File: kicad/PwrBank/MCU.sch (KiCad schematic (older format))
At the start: 2 parts

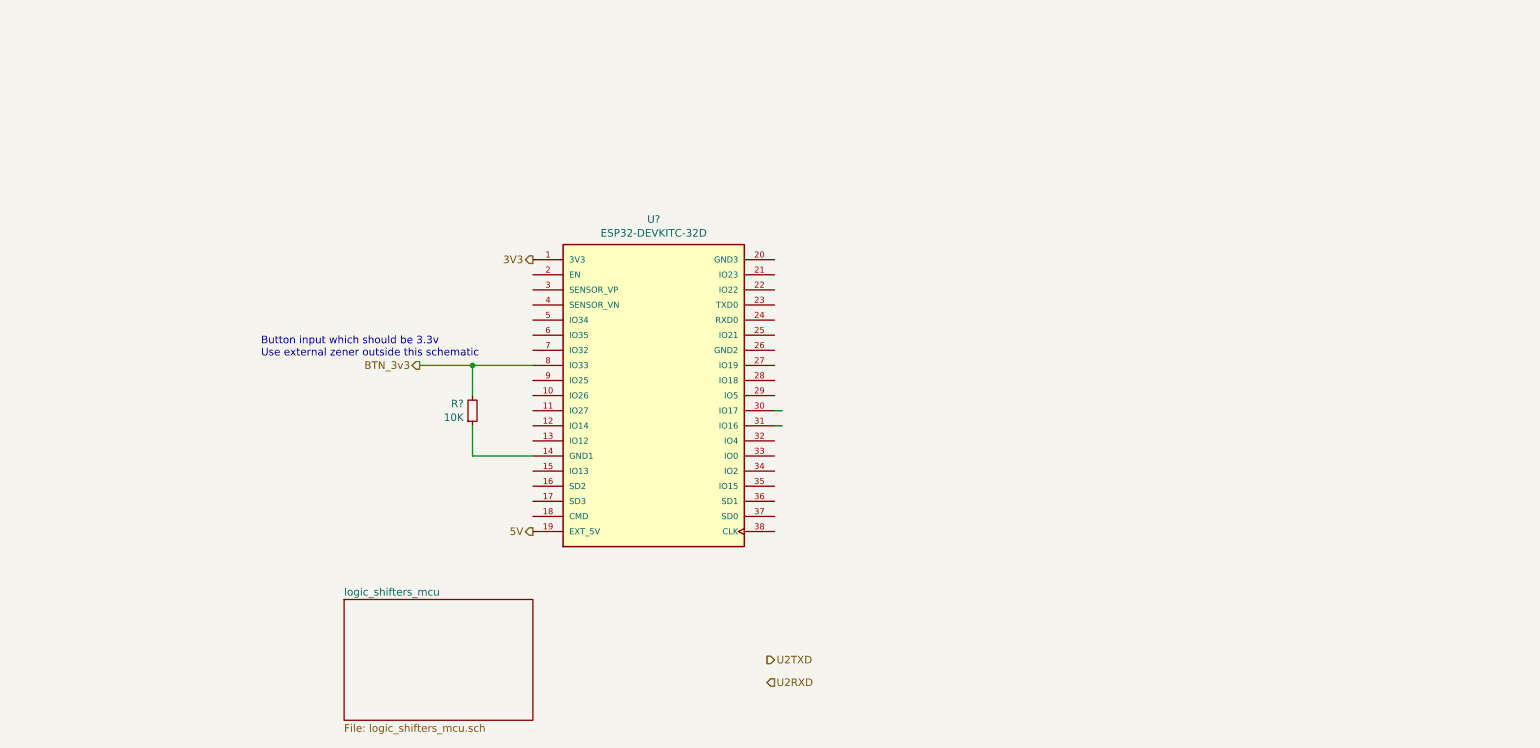
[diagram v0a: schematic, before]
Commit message: Working on/off system with safe shutdown and deepsleep inbetween
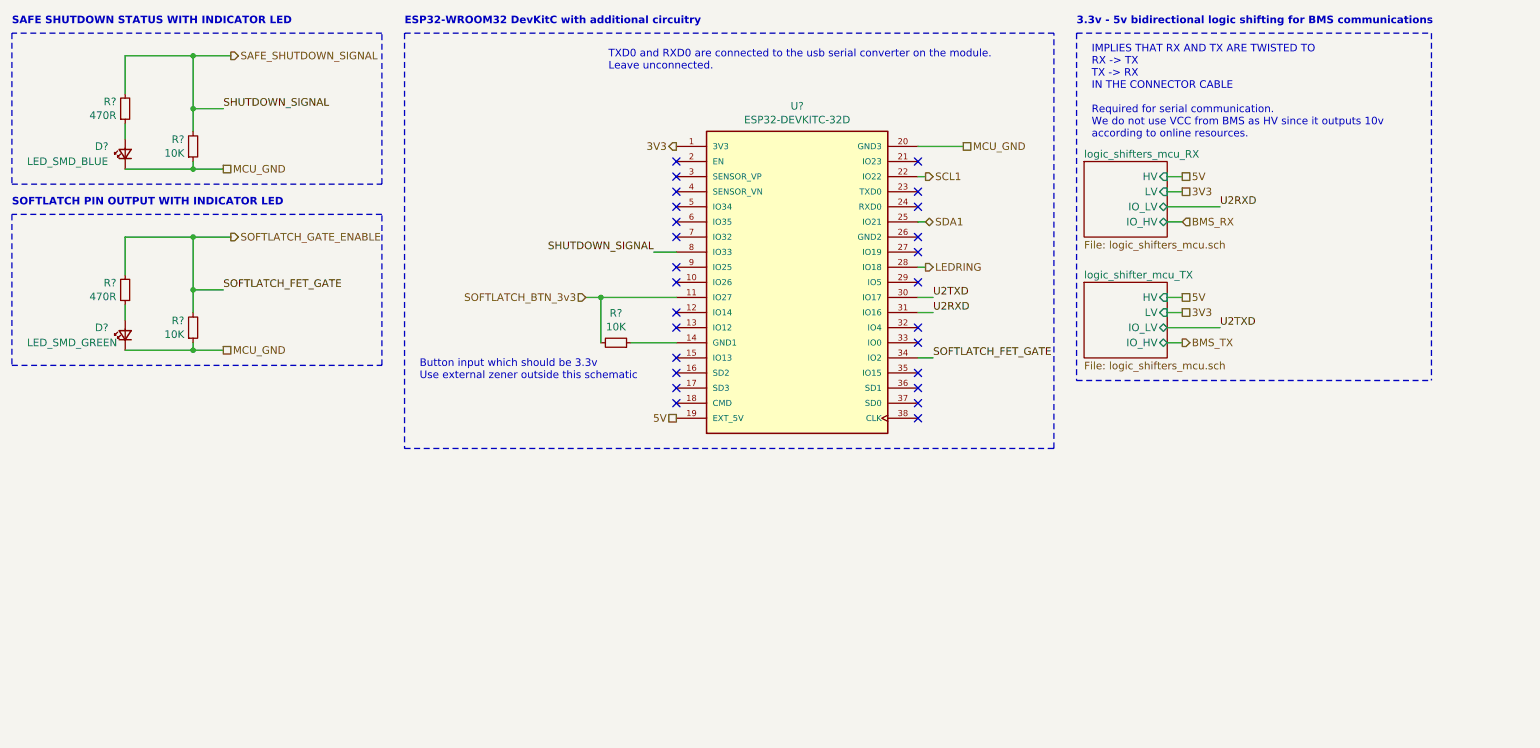
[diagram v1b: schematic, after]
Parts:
- added D?: LED_SMD_GREEN, symbol Device:LED_Small
- added D?: LED_SMD_BLUE, symbol Device:LED_Small
- added R? (x2): 10K, symbol Device:R_Small
- added R? (x2): 470R, symbol Device:R_Small
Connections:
- net labels added: BMS_RX, BMS_TX, LEDRING, MCU_GND, SAFE_SHUTDOWN_SIGNAL, SCL1, SDA1, SHUTDOWN_SIGNAL, SOFTLATCH_BTN_3v3, SOFTLATCH_FET_GATE, SOFTLATCH_GATE_ENABLE
- net labels removed: BTN_3v3
- wire segments 7 -> 40
- no-connect marks 0 -> 26
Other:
- note added: "3.3v - 5v bidirectional logic shifting for BMS communications"
- note added: "ESP32-WROOM32 DevKitC with additional circuitry\n"
- note added: "IMPLIES THAT RX AND TX ARE TWISTED TO\nRX -> TX\nTX -> RX\nIN THE CONNECTOR CABLE\n\nRequired for serial communication.\nWe do not use VCC from BMS as HV since it outputs 10v\naccording to online resources."
- note added: "SAFE SHUTDOWN STATUS WITH INDICATOR LED"
- note added: "SOFTLATCH PIN OUTPUT WITH INDICATOR LED"
- note added: "TXD0 and RXD0 are connected to the usb serial converter on the module.\nLeave unconnected."
- moved on the sheet: R?, U?

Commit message: UPDATE KICAD SOURCEFILES
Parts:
- R11, R12, R13, R14, R15: renamed from R?; footprint (none) -> Resistor_SMD:R_0805_2012Metric_Pad1.20x1.40mm_HandSolder
- U2: renamed from U?; footprint MODULE_ESP32-DEVKITC-32D -> ESP32-DEVKITC-32D:MODULE_ESP32-DEVKITC-32D
- gave numbers to parts that had none: 2
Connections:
- net 3V3 renamed +3V3
- net 5V renamed +5V
- net MCU_GND renamed GND
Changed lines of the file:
@@
 $Descr A4 11693 8268
 encoding utf-8
-Sheet 7 9
+Sheet 6 8
 Title "ESP32_Devkit_Addons"
 Date "2021-07-17"
@@
 $EndDescr
 $Comp
-L ESP32-DEVKITC-32D:ESP32-DEVKITC-32D U?
+L ESP32-DEVKITC-32D:ESP32-DEVKITC-32D U2
 U 1 1 60F2EDCB
 P 6050 2900
-F 0 "U?" H 6050 4067 50  0000 C CNN
+F 0 "U2" H 6050 4067 50  0000 C CNN
 F 1 "ESP32-DEVKITC-32D" H 6050 3976 50  0000 C CNN
-F 2 "MODULE_ESP32-DEVKITC-32D" H 6050 2900 50  0001 L BNN
+F 2 "ESP32-DEVKITC-32D:MODULE_ESP32-DEVKITC-32D" H 6050 2900 50  0001 L BNN
 F 3 "" H 6050 2900 50  0001 L BNN
 F 4 "4" H 6050 2900 50  0001 L BNN "PARTREV"
@@
 BMS_TX
 $Comp
-L Device:R_Small R?
+L Device:R_Small R15
 U 1 1 60F3049F
 P 4850 3300
-F 0 "R?" V 5046 3300 50  0000 C CNN
+F 0 "R15" V 5046 3300 50  0000 C CNN
 F 1 "10K" V 4955 3300 50  0000 C CNN
-F 2 "" H 4850 3300 50  0001 C CNN
+F 2 "Resistor_SMD:R_0805_2012Metric_Pad1.20x1.40mm_HandSolder" H 4850 3300 50  0001 C CNN
 F 3 "~" H 4850 3300 50  0001 C CNN
 	1    4850 3300
@@
 Text Notes 3550 3550 0    50   ~ 0
 Button input which should be 3.3v\nUse external zener outside this schematic
-Text HLabel 5250 3800 0    50   UnSpc ~ 0
-5V
-Text HLabel 5250 2000 0    50   Output ~ 0
-3V3
-$Sheet
-S 7950 2100 550  500
-U 60F3980E
-F0 "logic_shifters_mcu_RX" 50
-F1 "logic_shifters_mcu.sch" 50
-F2 "IO_LV" B R 8500 2400 50
-F3 "IO_HV" B R 8500 2500 50
-F4 "HV" I R 8500 2200 50
-F5 "LV" I R 8500 2300 50
-$EndSheet
-Text HLabel 8600 2200 2    50   UnSpc ~ 0
-5V
 Wire Wire Line
 	8600 2200 8500 2200
-Text HLabel 8600 3000 2    50   UnSpc ~ 0
-5V
 Wire Wire Line
 	8600 3000 8500 3000
-Text HLabel 8600 3100 2    50   UnSpc ~ 0
-3V3
 Wire Wire Line
 	8600 3100 8500 3100
-Text HLabel 8600 2300 2    50   UnSpc ~ 0
-3V3
 Wire Wire Line
 	8600 2300 8500 2300
@@
 Text Notes 7900 1200 0    50   ~ 10
 3.3v - 5v bidirectional logic shifting for BMS communications
-Text HLabel 7150 2000 2    50   UnSpc ~ 0
-MCU_GND
 Wire Wire Line
 	7150 2000 6850 2000
@@
 	4650 3000 4750 3000
 Wire Wire Line
-	5250 3300 4950 3300
+	5250 3300 5050 3300
 Wire Wire Line
 	4750 3300 4750 3000
@@
 	4750 3000 5250 3000
 $Comp
-L Device:LED_Small D?
+L Device:LED_Small D3
 U 1 1 60F6DAA2
 P 1600 2050
-F 0 "D?" V 1650 2250 50  0000 R CNN
+F 0 "D3" V 1650 2250 50  0000 R CNN
 F 1 "LED_SMD_BLUE" V 1550 2700 50  0000 R CNN
 F 2 "" V 1600 2050 50  0001 C CNN
@@
 Wire Wire Line
 	5100 2700 5250 2700
-Text HLabel 2250 2150 2    50   UnSpc ~ 0
-MCU_GND
 Text Label 2250 1750 0    50   ~ 0
 SHUTDOWN_SIGNAL
@@
 	2300 1400 2050 1400
 $Comp
-L Device:R_Small R?
+L Device:R_Small R13
 U 1 1 60F71BF4
 P 2050 2000
-F 0 "R?" H 1992 1954 50  0000 R CNN
+F 0 "R13" H 1992 1954 50  0000 R CNN
 F 1 "10K" H 1992 2045 50  0000 R CNN
-F 2 "" H 2050 2000 50  0001 C CNN
+F 2 "Resistor_SMD:R_0805_2012Metric_Pad1.20x1.40mm_HandSolder" H 2050 2000 50  0001 C CNN
 F 3 "~" H 2050 2000 50  0001 C CNN
 	1    2050 2000
@@
 	1600 2150 2050 2150
 $Comp
-L Device:R_Small R?
+L Device:R_Small R11
 U 1 1 60F80C8C
 P 1600 1750
-F 0 "R?" H 1542 1704 50  0000 R CNN
+F 0 "R11" H 1542 1704 50  0000 R CNN
 F 1 "470R" H 1542 1795 50  0000 R CNN
-F 2 "" H 1600 1750 50  0001 C CNN
+F 2 "Resistor_SMD:R_0805_2012Metric_Pad1.20x1.40mm_HandSolder" H 1600 1750 50  0001 C CNN
 F 3 "~" H 1600 1750 50  0001 C CNN
 	1    1600 1750
@@
 	6950 3400 6850 3400
 $Comp
-L Device:LED_Small D?
+L Device:LED_Small D4
 U 1 1 60F351C2
 P 1600 3250
-F 0 "D?" V 1650 3450 50  0000 R CNN
+F 0 "D4" V 1650 3450 50  0000 R CNN
 F 1 "LED_SMD_GREEN" V 1550 3900 50  0000 R CNN
 F 2 "" V 1600 3250 50  0001 C CNN
@@
 	0    -1   -1   0
 $EndComp
-Text HLabel 2250 3350 2    50   UnSpc ~ 0
-MCU_GND
 Text Label 2250 2950 0    50   ~ 0
 SOFTLATCH_FET_GATE
@@
 	2300 2600 2050 2600
 $Comp
-L Device:R_Small R?
+L Device:R_Small R14
 U 1 1 60F351CF
 P 2050 3200
-F 0 "R?" H 1992 3154 50  0000 R CNN
+F 0 "R14" H 1992 3154 50  0000 R CNN
 F 1 "10K" H 1992 3245 50  0000 R CNN
-F 2 "" H 2050 3200 50  0001 C CNN
+F 2 "Resistor_SMD:R_0805_2012Metric_Pad1.20x1.40mm_HandSolder" H 2050 3200 50  0001 C CNN
 F 3 "~" H 2050 3200 50  0001 C CNN
 	1    2050 3200
@@
 	1600 3350 2050 3350
 $Comp
-L Device:R_Small R?
+L Device:R_Small R12
 U 1 1 60F351DA
 P 1600 2950
-F 0 "R?" H 1542 2904 50  0000 R CNN
+F 0 "R12" H 1542 2904 50  0000 R CNN
 F 1 "470R" H 1542 2995 50  0000 R CNN
-F 2 "" H 1600 2950 50  0001 C CNN
+F 2 "Resistor_SMD:R_0805_2012Metric_Pad1.20x1.40mm_HandSolder" H 1600 2950 50  0001 C CNN
 F 3 "~" H 1600 2950 50  0001 C CNN
 	1    1600 2950
@@
 Text Notes 3450 1200 0    50   ~ 10
 ESP32-WROOM32 DevKitC with additional circuitry\n
+Wire Wire Line
+	5250 2000 5150 2000
+Wire Wire Line
+	5150 3800 5250 3800
+$Comp
+L power:GND #PWR027
+U 1 1 61034275
+P 7150 2000
+F 0 "#PWR027" H 7150 1750 50  0001 C CNN
+F 1 "GND" V 7155 1872 50  0000 R CNN
+F 2 "" H 7150 2000 50  0001 C CNN
+F 3 "" H 7150 2000 50  0001 C CNN
+	1    7150 2000
+	0    -1   -1   0
+$EndComp
+$Comp
+L power:GND #PWR023
+U 1 1 61035069
+P 2250 2150
+F 0 "#PWR023" H 2250 1900 50  0001 C CNN
+F 1 "GND" V 2255 2022 50  0000 R CNN
+F 2 "" H 2250 2150 50  0001 C CNN
+F 3 "" H 2250 2150 50  0001 C CNN
+	1    2250 2150
+	0    -1   -1   0
+$EndComp
+$Comp
+L power:GND #PWR024
+U 1 1 61035606
+P 2250 3350
+F 0 "#PWR024" H 2250 3100 50  0001 C CNN
+F 1 "GND" V 2255 3222 50  0000 R CNN
+F 2 "" H 2250 3350 50  0001 C CNN
+F 3 "" H 2250 3350 50  0001 C CNN
+	1    2250 3350
+	0    -1   -1   0
+$EndComp
+$Comp
+L power:+3.3V #PWR025
+U 1 1 61037CC9
+P 5150 2000
+F 0 "#PWR025" H 5150 1850 50  0001 C CNN
+F 1 "+3.3V" V 5165 2128 50  0000 L CNN
+F 2 "" H 5150 2000 50  0001 C CNN
+F 3 "" H 5150 2000 50  0001 C CNN
+	1    5150 2000
+	0    -1   -1   0
+$EndComp
+$Comp
+L power:+5V #PWR026
+U 1 1 61038914
+P 5150 3800
+F 0 "#PWR026" H 5150 3650 50  0001 C CNN
+F 1 "+5V" V 5165 3928 50  0000 L CNN
+F 2 "" H 5150 3800 50  0001 C CNN
+F 3 "" H 5150 3800 50  0001 C CNN
+	1    5150 3800
+	0    -1   -1   0
+$EndComp
+$Sheet
+S 7950 2100 550  500
+U 60F3980E
+F0 "logic_shifters_mcu_RX" 50
+F1 "logic_shifters_mcu.sch" 50
+F2 "IO_LV" B R 8500 2400 50
+F3 "IO_HV" B R 8500 2500 50
+F4 "HV" I R 8500 2200 50
+F5 "LV" I R 8500 2300 50
+$EndSheet
+$Comp
+L power:+5V #PWR028
+U 1 1 61039E33
+P 8600 2200
+F 0 "#PWR028" H 8600 2050 50  0001 C CNN
+F 1 "+5V" V 8615 2328 50  0000 L CNN
+F 2 "" H 8600 2200 50  0001 C CNN
+F 3 "" H 8600 2200 50  0001 C CNN
+	1    8600 2200
+	0    1    1    0
+$EndComp
+$Comp
+L power:+3.3V #PWR029
+U 1 1 6103A5D9
+P 8600 2300
+F 0 "#PWR029" H 8600 2150 50  0001 C CNN
+F 1 "+3.3V" V 8615 2428 50  0000 L CNN
+F 2 "" H 8600 2300 50  0001 C CNN
+F 3 "" H 8600 2300 50  0001 C CNN
+	1    8600 2300
+	0    1    1    0
+$EndComp
+$Comp
+L power:+5V #PWR030
+U 1 1 6103DF7E
+P 8600 3000
+F 0 "#PWR030" H 8600 2850 50  0001 C CNN
+F 1 "+5V" V 8615 3128 50  0000 L CNN
+F 2 "" H 8600 3000 50  0001 C CNN
+F 3 "" H 8600 3000 50  0001 C CNN
+	1    8600 3000
+	0    1    1    0
+$EndComp
+$Comp
+L power:+3.3V #PWR031
+U 1 1 6103E675
+P 8600 3100
+F 0 "#PWR031" H 8600 2950 50  0001 C CNN
+F 1 "+3.3V" V 8615 3228 50  0000 L CNN
+F 2 "" H 8600 3100 50  0001 C CNN
+F 3 "" H 8600 3100 50  0001 C CNN
+	1    8600 3100
+	0    1    1    0
+$EndComp
+$Comp
+L power:PWR_FLAG #FLG06
+U 1 1 6109BF9C
+P 2250 2150
+F 0 "#FLG06" H 2250 2225 50  0001 C CNN
+F 1 "PWR_FLAG" H 2250 2323 50  0000 C CNN
+F 2 "" H 2250 2150 50  0001 C CNN
+F 3 "~" H 2250 2150 50  0001 C CNN
+	1    2250 2150
+	1    0    0    -1
+$EndComp
+Connection ~ 2250 2150
+$Comp
+L power:PWR_FLAG #FLG08
+U 1 1 6109CF19
+P 9050 3000
+F 0 "#FLG08" H 9050 3075 50  0001 C CNN
+F 1 "PWR_FLAG" V 9050 3128 50  0000 L CNN
+F 2 "" H 9050 3000 50  0001 C CNN
+F 3 "~" H 9050 3000 50  0001 C CNN
+	1    9050 3000
+	0    1    1    0
+$EndComp
+Wire Wire Line
+	9050 3000 9000 3000
+Wire Wire Line
+	9000 3000 9000 2950
+Wire Wire Line
+	9000 2950 8600 2950
+Wire Wire Line
+	8600 2950 8600 3000
+Connection ~ 8600 3000
+$Comp
+L power:PWR_FLAG #FLG07
+U 1 1 610A25D9
+P 5050 3300
+F 0 "#FLG07" H 5050 3375 50  0001 C CNN
+F 1 "PWR_FLAG" H 5050 3473 50  0000 C CNN
+F 2 "" H 5050 3300 50  0001 C CNN
+F 3 "~" H 5050 3300 50  0001 C CNN
+	1    5050 3300
+	1    0    0    -1
+$EndComp
+Connection ~ 5050 3300
+Wire Wire Line
+	5050 3300 4950 3300
 $EndSCHEMATC

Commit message: Kicad files update
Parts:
- renumbered R13 to R10, R14 to R11, R15 to R12, R11 to R8, R12 to R9
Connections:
- net SDA2: now reaches U2.27 (IO19)
- net LEDRING renamed SCL2
- no-connect marks 26 -> 25
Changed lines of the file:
@@
 $Descr A4 11693 8268
 encoding utf-8
-Sheet 6 8
+Sheet 6 9
 Title "ESP32_Devkit_Addons"
 Date "2021-07-17"
@@
 BMS_TX
 $Comp
-L Device:R_Small R15
+L Device:R_Small R12
 U 1 1 60F3049F
 P 4850 3300
-F 0 "R15" V 5046 3300 50  0000 C CNN
+F 0 "R12" V 5046 3300 50  0000 C CNN
 F 1 "10K" V 4955 3300 50  0000 C CNN
 F 2 "Resistor_SMD:R_0805_2012Metric_Pad1.20x1.40mm_HandSolder" H 4850 3300 50  0001 C CNN
@@
 	2300 1400 2050 1400
 $Comp
-L Device:R_Small R13
+L Device:R_Small R10
 U 1 1 60F71BF4
 P 2050 2000
-F 0 "R13" H 1992 1954 50  0000 R CNN
+F 0 "R10" H 1992 1954 50  0000 R CNN
 F 1 "10K" H 1992 2045 50  0000 R CNN
 F 2 "Resistor_SMD:R_0805_2012Metric_Pad1.20x1.40mm_HandSolder" H 2050 2000 50  0001 C CNN
@@
 	1600 2150 2050 2150
 $Comp
-L Device:R_Small R11
+L Device:R_Small R8
 U 1 1 60F80C8C
 P 1600 1750
-F 0 "R11" H 1542 1704 50  0000 R CNN
+F 0 "R8" H 1542 1704 50  0000 R CNN
 F 1 "470R" H 1542 1795 50  0000 R CNN
 F 2 "Resistor_SMD:R_0805_2012Metric_Pad1.20x1.40mm_HandSolder" H 1600 1750 50  0001 C CNN
@@
 	2300 2600 2050 2600
 $Comp
-L Device:R_Small R14
+L Device:R_Small R11
 U 1 1 60F351CF
 P 2050 3200
-F 0 "R14" H 1992 3154 50  0000 R CNN
+F 0 "R11" H 1992 3154 50  0000 R CNN
 F 1 "10K" H 1992 3245 50  0000 R CNN
 F 2 "Resistor_SMD:R_0805_2012Metric_Pad1.20x1.40mm_HandSolder" H 2050 3200 50  0001 C CNN
@@
 	1600 3350 2050 3350
 $Comp
-L Device:R_Small R12
+L Device:R_Small R9
 U 1 1 60F351DA
 P 1600 2950
-F 0 "R12" H 1542 2904 50  0000 R CNN
+F 0 "R9" H 1542 2904 50  0000 R CNN
 F 1 "470R" H 1542 2995 50  0000 R CNN
 F 2 "Resistor_SMD:R_0805_2012Metric_Pad1.20x1.40mm_HandSolder" H 1600 2950 50  0001 C CNN
@@
 Wire Wire Line
 	6900 2800 6850 2800
-Text HLabel 6900 2800 2    50   Output ~ 0
-LEDRING
 Text HLabel 6900 2500 2    50   BiDi ~ 0
 SDA1
@@
 NoConn ~ 6850 3200
 NoConn ~ 6850 2900
-NoConn ~ 6850 2700
 NoConn ~ 6850 2600
 NoConn ~ 6850 2100
@@
 	5150 3800 5250 3800
 $Comp
-L power:GND #PWR027
+L power:GND #PWR029
 U 1 1 61034275
 P 7150 2000
-F 0 "#PWR027" H 7150 1750 50  0001 C CNN
+F 0 "#PWR029" H 7150 1750 50  0001 C CNN
 F 1 "GND" V 7155 1872 50  0000 R CNN
 F 2 "" H 7150 2000 50  0001 C CNN
@@
 $EndComp
 $Comp
-L power:GND #PWR023
+L power:GND #PWR025
 U 1 1 61035069
 P 2250 2150
-F 0 "#PWR023" H 2250 1900 50  0001 C CNN
+F 0 "#PWR025" H 2250 1900 50  0001 C CNN
 F 1 "GND" V 2255 2022 50  0000 R CNN
 F 2 "" H 2250 2150 50  0001 C CNN
@@
 $EndComp
 $Comp
-L power:GND #PWR024
+L power:GND #PWR026
 U 1 1 61035606
 P 2250 3350
-F 0 "#PWR024" H 2250 3100 50  0001 C CNN
+F 0 "#PWR026" H 2250 3100 50  0001 C CNN
 F 1 "GND" V 2255 3222 50  0000 R CNN
 F 2 "" H 2250 3350 50  0001 C CNN
@@
 $EndComp
 $Comp
-L power:+3.3V #PWR025
+L power:+3.3V #PWR027
 U 1 1 61037CC9
 P 5150 2000
-F 0 "#PWR025" H 5150 1850 50  0001 C CNN
+F 0 "#PWR027" H 5150 1850 50  0001 C CNN
 F 1 "+3.3V" V 5165 2128 50  0000 L CNN
 F 2 "" H 5150 2000 50  0001 C CNN
@@
 $EndComp
 $Comp
-L power:+5V #PWR026
+L power:+5V #PWR028
 U 1 1 61038914
 P 5150 3800
-F 0 "#PWR026" H 5150 3650 50  0001 C CNN
+F 0 "#PWR028" H 5150 3650 50  0001 C CNN
 F 1 "+5V" V 5165 3928 50  0000 L CNN
 F 2 "" H 5150 3800 50  0001 C CNN
@@
 $EndSheet
 $Comp
-L power:+5V #PWR028
+L power:+5V #PWR030
 U 1 1 61039E33
 P 8600 2200
-F 0 "#PWR028" H 8600 2050 50  0001 C CNN
+F 0 "#PWR030" H 8600 2050 50  0001 C CNN
 F 1 "+5V" V 8615 2328 50  0000 L CNN
 F 2 "" H 8600 2200 50  0001 C CNN
@@
 $EndComp
 $Comp
-L power:+3.3V #PWR029
+L power:+3.3V #PWR031
 U 1 1 6103A5D9
 P 8600 2300
-F 0 "#PWR029" H 8600 2150 50  0001 C CNN
+F 0 "#PWR031" H 8600 2150 50  0001 C CNN
 F 1 "+3.3V" V 8615 2428 50  0000 L CNN
 F 2 "" H 8600 2300 50  0001 C CNN
@@
 $EndComp
 $Comp
-L power:+5V #PWR030
+L power:+5V #PWR032
 U 1 1 6103DF7E
 P 8600 3000
-F 0 "#PWR030" H 8600 2850 50  0001 C CNN
+F 0 "#PWR032" H 8600 2850 50  0001 C CNN
 F 1 "+5V" V 8615 3128 50  0000 L CNN
 F 2 "" H 8600 3000 50  0001 C CNN
@@
 $EndComp
 $Comp
-L power:+3.3V #PWR031
+L power:+3.3V #PWR033
 U 1 1 6103E675
 P 8600 3100
-F 0 "#PWR031" H 8600 2950 50  0001 C CNN
+F 0 "#PWR033" H 8600 2950 50  0001 C CNN
 F 1 "+3.3V" V 8615 3228 50  0000 L CNN
 F 2 "" H 8600 3100 50  0001 C CNN
@@
 Wire Wire Line
 	5050 3300 4950 3300
+Text HLabel 6900 2800 2    50   Output ~ 0
+SCL2
+Text HLabel 6850 2700 2    50   BiDi ~ 0
+SDA2
 $EndSCHEMATC
